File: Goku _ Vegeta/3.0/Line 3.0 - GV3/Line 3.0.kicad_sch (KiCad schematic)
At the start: 109 parts, among them J1 BATTERY POWER, J10 RIGHT HEADERS, J11 I2C, J3 Motor 1, J4 Motor 3, J5 Kicker Voltmeter, J6 Solenoid, J7 Motor 2, J8 Motor 4, J9 LEFT HEADERS, Q1 BSC040N10NS5, U1 TPS62132, U2 TPS62133, U4 TB67H420FTG Dual/Single Motor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, U5 TB67H420FTG Dual/Single Motor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, U6 LM2587S-ADJ, U7 TB67H420FTG Dual/Single Motor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, U8 TB67H420FTG Dual/Single Motor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, U9 DEV-16771

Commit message: Line 3.0 save
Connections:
- net SEN10 is gone; now on net 38: A10.2, R26.2
- net SEN11 is gone; now on net 39: A11.2, R27.2
- net SEN12 is gone; now on net 40: A12.2, R28.2
- net SEN13 is gone; now on net 41: A13.2, R29.2
- net SEN2 is gone; now on net 26: A2.2, R10.2
- net SEN3 is gone; now on net 24: A3.2, R11.2
- net SEN6 is gone; now on net 27: A6.2, R14.2
- net SEN7 is gone; now on net 25: A7.2, R15.2
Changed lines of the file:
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@@
     (effects (font (size 1.27 1.27)) (justify right bottom))
   )
-  (label "SEN11" (at 275.59 226.06 0) (fields_autoplaced)
-    (effects (font (size 1.27 1.27)) (justify left bottom))
+  (label "SEN11" (at 386.08 205.74 180) (fields_autoplaced)
+    (effects (font (size 1.27 1.27)) (justify right bottom))
   )
   (label "16" (at 327.66 200.66 0) (fields_autoplaced)
     (effects (font (size 1.27 1.27)) (justify left bottom))
   )
-  (label "SEN12" (at 275.59 228.6 0) (fields_autoplaced)
-    (effects (font (size 1.27 1.27)) (justify left bottom))
+  (label "SEN12" (at 386.08 203.2 180) (fields_autoplaced)
+    (effects (font (size 1.27 1.27)) (justify right bottom))
   )
   (label "30" (at 327.66 175.26 0) (fields_autoplaced)
@@
     (effects (font (size 1.27 1.27)) (justify left bottom))
   )
-  (label "SEN13" (at 275.59 231.14 0) (fields_autoplaced)
-    (effects (font (size 1.27 1.27)) (justify left bottom))
+  (label "SEN13" (at 386.08 200.66 180) (fields_autoplaced)
+    (effects (font (size 1.27 1.27)) (justify right bottom))
   )
   (label "41" (at 393.7 186.69 0) (fields_autoplaced)
@@
     (effects (font (size 1.27 1.27)) (justify left bottom))
   )
-  (label "SEN3" (at 275.59 205.74 0) (fields_autoplaced)
-    (effects (font (size 1.27 1.27)) (justify left bottom))
+  (label "SEN3" (at 386.08 218.44 180) (fields_autoplaced)
+    (effects (font (size 1.27 1.27)) (justify right bottom))
   )
   (label "12" (at 309.88 180.34 180) (fields_autoplaced)
@@
     (effects (font (size 1.27 1.27)) (justify left bottom))
   )
-  (label "SEN10" (at 275.59 223.52 0) (fields_autoplaced)
-    (effects (font (size 1.27 1.27)) (justify left bottom))
+  (label "SEN10" (at 386.08 208.28 180) (fields_autoplaced)
+    (effects (font (size 1.27 1.27)) (justify right bottom))
   )
   (label "M1ENCA" (at 275.59 180.34 0) (fields_autoplaced)
@@
     (effects (font (size 1.27 1.27)) (justify right bottom))
   )
-  (label "SEN7" (at 275.59 215.9 0) (fields_autoplaced)
-    (effects (font (size 1.27 1.27)) (justify left bottom))
+  (label "SEN7" (at 386.08 215.9 180) (fields_autoplaced)
+    (effects (font (size 1.27 1.27)) (justify right bottom))
   )
   (label "M3IN1" (at 275.59 254 0) (fields_autoplaced)
@@
     (effects (font (size 1.27 1.27)) (justify right bottom))
   )
-  (label "SEN2" (at 275.59 203.2 0) (fields_autoplaced)
-    (effects (font (size 1.27 1.27)) (justify left bottom))
+  (label "SEN2" (at 386.08 213.36 180) (fields_autoplaced)
+    (effects (font (size 1.27 1.27)) (justify right bottom))
   )
   (label "15" (at 393.7 176.53 0) (fields_autoplaced)
@@
     (effects (font (size 1.27 1.27)) (justify right bottom))
   )
-  (label "SEN6" (at 275.59 213.36 0) (fields_autoplaced)
-    (effects (font (size 1.27 1.27)) (justify left bottom))
+  (label "SEN6" (at 386.08 210.82 180) (fields_autoplaced)
+    (effects (font (size 1.27 1.27)) (justify right bottom))
   )
   (label "10" (at 309.88 175.26 180) (fields_autoplaced)

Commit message: CLEAN UP 3.0 LINE SCH
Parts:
- added J2: BACKUP 5V, Connector_AMASS:AMASS_XT30U-F_1x02_P5.0mm_Vertical, symbol Connector:Conn_01x02_Male
- added J3: BACKUP 3V3, Connector_AMASS:AMASS_XT30U-F_1x02_P5.0mm_Vertical, symbol Connector:Conn_01x02_Male
- renumbered C11 to C10, C12 to C11, C13 to C12, C14 to C13, C6 to C5, C7 to C6, C8 to C7, C9 to C8, C10 to C9, J8 to J10, J9 to J11, J10 to J12, J11 to J4, J3 to J7, J7 to J8, J4 to J9, R34 to R33, R35 to R34, R36 to R35, R37 to R36, R38 to R37, R39 to R38, U6 to U3, U7 to U5, U5 to U6, U8 to U7, U9 to U8
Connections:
- net KICKERTRIG is gone; now on net 13: Q1.4 (G)
- net M1ENCA is gone; now on net 7: J7.5 (Pin_5)
- net M1ENCB is gone; now on net 8: J7.6 (Pin_6)
- net M1IN1 is gone; now on net 2: U4.4 (INA1)
- net M1IN2 is gone; now on net 6: U4.5 (INA2)
- net M1PWM is gone; now on net 28: U4.6 (PWMA)
- net M2ENCA is gone; now on net 34: J8.5 (Pin_5)
- net M2ENCB is gone; now on net 35: J8.6 (Pin_6)
- net M2IN1 is gone; now on net 9: U5.4 (INA1)
- net M2IN2 is gone; now on net 32: U5.5 (INA2)
- net M2PWM is gone; now on net 29: U5.6 (PWMA)
- net M3ENCA is gone; now on net 30: J9.5 (Pin_5)
- net M3ENCB is gone; now on net 31: J9.6 (Pin_6)
- net M3IN1 is gone; now on net 10: U6.4 (INA1)
- net M3IN2 is gone; now on net 12: U6.5 (INA2)
- net M3PWM is gone; now on net 37: U6.6 (PWMA)
- net M4ENCA is gone; now on net 3: J10.5 (Pin_5)
- net M4ENCB is gone; now on net 4: J10.6 (Pin_6)
- net M4IN1 is gone; now on net 11: U7.4 (INA1)
- net M4IN2 is gone; now on net 33: U7.5 (INA2)
- net M4PWM is gone; now on net 36: U7.6 (PWMA)
- net SEN14 is gone; now on net 14: A14.2, R30.2
- net SEN15 is gone; now on net 15: A15.2, R31.2
- net +15V: now also J2.1 (Pin_1), J3.1 (Pin_1)
- net GND: now also C2.2, C4.2, C6.1, U2.6 (AGND), U2.7 (FSW), U2.8 (DEF), J2.2 (Pin_2), J3.2 (Pin_2)
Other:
- moved on the sheet: C1, C10, C11, C12, C13, C2, C3, C4, C5, C6, C7, C8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

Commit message: line 3.0 - good for the night
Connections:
- net +15V: now also J1.2 (Pin_2); no longer J1.1 (Pin_1), J2.1 (Pin_1), J3.1 (Pin_1)
- net +3V3: now also J3.2 (Pin_2)
- net +5V: now also J2.2 (Pin_2)
- net 18: now also J4.2 (Pin_2); no longer J4.1 (Pin_1)
- net 19: now also J4.1 (Pin_1); no longer J4.2 (Pin_2)
- net GND: now also J1.1 (Pin_1), J2.1 (Pin_1), J3.1 (Pin_1); no longer J1.2 (Pin_2), J2.2 (Pin_2), J3.2 (Pin_2)
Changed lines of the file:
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@@
     (fill (type none))
   )
-  (rectangle (start 107.95 19.05) (end 139.7 67.31)
+  (rectangle (start 107.95 19.05) (end 139.7 68.58)
     (stroke (width 0) (type dash))
     (fill (type none))
@@
     )
   )
-  (symbol (lib_id "power:+15V") (at 130.81 53.34 0) (unit 1)
-    (in_bom yes) (on_board yes) (dnp no)
-    (property "Reference" "#PWR053" (at 130.81 57.15 0)
-      (effects (font (size 1.27 1.27)) hide)
-    )
-    (property "Value" "+15V" (at 130.81 49.53 0)
-      (effects (font (size 1.27 1.27)))
-    )
-    (property "Footprint" "" (at 130.81 53.34 0)
-      (effects (font (size 1.27 1.27)) hide)
-    )
-    (property "Datasheet" "" (at 130.81 53.34 0)
-      (effects (font (size 1.27 1.27)) hide)
-    )
-    (pin "1")
-    (instances
-      (project "Line 3.0"
-        (path "/d5c7bd24-918a-4dd6-9ba7-d38579daba08"
-          (reference "#PWR053") (unit 1)
-        )
-      )
-    )
-  )
   (symbol (lib_id "JB2835AWT-W-U30GA0000-N0000001:JB2835AWT-W-U30GA0000-N0000001") (at 24.13 252.73 90) (mirror x) (unit 1)
     (in_bom yes) (on_board yes) (dnp no)
@@
     )
   )
-  (symbol (lib_id "Connector:Conn_01x02_Male") (at 118.11 40.64 0) (unit 1)
-    (in_bom yes) (on_board yes) (dnp no) (fields_autoplaced)
-    (property "Reference" "J2" (at 118.745 35.56 0)
+  (symbol (lib_id "Connector:Conn_01x02_Male") (at 118.11 43.18 0) (mirror x) (unit 1)
+    (in_bom yes) (on_board yes) (dnp no)
+    (property "Reference" "J2" (at 118.11 38.1 0)
       (effects (font (size 1.27 1.27)))
     )
-    (property "Value" "BACKUP 5V" (at 118.745 38.1 0)
+    (property "Value" "BACKUP 5V" (at 118.11 35.56 0)
       (effects (font (size 1.27 1.27)))
     )
-    (property "Footprint" "Connector_AMASS:AMASS_XT30U-F_1x02_P5.0mm_Vertical" (at 118.11 40.64 0)
+    (property "Footprint" "Connector_AMASS:AMASS_XT30U-F_1x02_P5.0mm_Vertical" (at 118.11 43.18 0)
       (effects (font (size 1.27 1.27)) hide)
     )
-    (property "Datasheet" "~" (at 118.11 40.64 0)
+    (property "Datasheet" "~" (at 118.11 43.18 0)
       (effects (font (size 1.27 1.27)) hide)
     )
@@
     )
   )
+  (symbol (lib_id "power:+3V3") (at 130.81 53.34 0) (unit 1)
+    (in_bom yes) (on_board yes) (dnp no)
+    (property "Reference" "#PWR051" (at 130.81 57.15 0)
+      (effects (font (size 1.27 1.27)) hide)
+    )
+    (property "Value" "+3V3" (at 130.81 49.53 0)
+      (effects (font (size 1.27 1.27)))
+    )
+    (property "Footprint" "" (at 130.81 53.34 0)
+      (effects (font (size 1.27 1.27)) hide)
+    )
+    (property "Datasheet" "" (at 130.81 53.34 0)
+      (effects (font (size 1.27 1.27)) hide)
+    )
+    (pin "1")
+    (instances
+      (project "Line 3.0"
+        (path "/d5c7bd24-918a-4dd6-9ba7-d38579daba08"
+          (reference "#PWR051") (unit 1)
+        )
+      )
+    )
+  )
   (symbol (lib_id "Device:R_Small_US") (at 24.13 91.44 0) (unit 1)
     (in_bom yes) (on_board yes) (dnp no)
@@
     )
   )
-  (symbol (lib_id "Connector:Conn_01x02_Male") (at 118.11 27.94 0) (unit 1)
-    (in_bom yes) (on_board yes) (dnp no) (fields_autoplaced)
-    (property "Reference" "J1" (at 118.745 22.86 0)
+  (symbol (lib_id "Connector:Conn_01x02_Male") (at 118.11 30.48 0) (mirror x) (unit 1)
+    (in_bom yes) (on_board yes) (dnp no)
+    (property "Reference" "J1" (at 117.475 25.4 0)
       (effects (font (size 1.27 1.27)))
     )
-    (property "Value" "BATTERY POWER" (at 118.745 25.4 0)
+    (property "Value" "BATTERY POWER" (at 118.11 21.59 0)
       (effects (font (size 1.27 1.27)))
     )
-    (property "Footprint" "Connector_AMASS:AMASS_XT60-F_1x02_P7.20mm_Vertical" (at 118.11 27.94 0)
+    (property "Footprint" "Connector_AMASS:AMASS_XT60-F_1x02_P7.20mm_Vertical" (at 118.11 30.48 0)
       (effects (font (size 1.27 1.27)) hide)
     )
-    (property "Datasheet" "~" (at 118.11 27.94 0)
+    (property "Datasheet" "~" (at 118.11 30.48 0)
       (effects (font (size 1.27 1.27)) hide)
     )
@@
     )
   )
+  (symbol (lib_name "+5V_1") (lib_id "power:+5V") (at 130.81 40.64 0) (unit 1)
+    (in_bom yes) (on_board yes) (dnp no)
+    (property "Reference" "#PWR053" (at 130.81 44.45 0)
+      (effects (font (size 1.27 1.27)) hide)
+    )
+    (property "Value" "+5V" (at 130.81 36.83 0)
+      (effects (font (size 1.27 1.27)))
+    )
+    (property "Footprint" "" (at 130.81 40.64 0)
+      (effects (font (size 1.27 1.27)) hide)
+    )
+    (property "Datasheet" "" (at 130.81 40.64 0)
+      (effects (font (size 1.27 1.27)) hide)
+    )
+    (pin "1")
+    (instances
+      (project "Line 3.0"
+        (path "/d5c7bd24-918a-4dd6-9ba7-d38579daba08"
+          (reference "#PWR053") (unit 1)
+        )
+      )
+    )
+  )
   (symbol (lib_id "ALS-PT19-315C_L177_TR8:ALS-PT19-315C{slash}L177{slash}TR8") (at 34.29 121.92 0) (mirror y) (unit 1)
     (in_bom yes) (on_board yes) (dnp no)
@@
     )
   )
-  (symbol (lib_id "Connector:Conn_01x02_Male") (at 118.11 64.77 0) (unit 1)
-    (in_bom yes) (on_board yes) (dnp no) (fields_autoplaced)
-    (property "Reference" "J4" (at 118.745 59.69 0)
+  (symbol (lib_id "Connector:Conn_01x02_Male") (at 118.11 67.31 0) (mirror x) (unit 1)
+    (in_bom yes) (on_board yes) (dnp no)
+    (property "Reference" "J4" (at 118.11 62.23 0)
       (effects (font (size 1.27 1.27)))
     )
-    (property "Value" "I2C" (at 118.745 62.23 0)
+    (property "Value" "I2C" (at 118.11 59.69 0)
       (effects (font (size 1.27 1.27)))
     )
-    (property "Footprint" "Connector_AMASS:AMASS_XT30U-F_1x02_P5.0mm_Vertical" (at 118.11 64.77 0)
+    (property "Footprint" "Connector_AMASS:AMASS_XT30U-F_1x02_P5.0mm_Vertical" (at 118.11 67.31 0)
       (effects (font (size 1.27 1.27)) hide)
     )
-    (property "Datasheet" "~" (at 118.11 64.77 0)
+    (property "Datasheet" "~" (at 118.11 67.31 0)
       (effects (font (size 1.27 1.27)) hide)
     )
@@
     )
   )
-  (symbol (lib_id "power:+15V") (at 130.81 40.64 0) (unit 1)
-    (in_bom yes) (on_board yes) (dnp no)
-    (property "Reference" "#PWR051" (at 130.81 44.45 0)
-      (effects (font (size 1.27 1.27)) hide)
-    )
-    (property "Value" "+15V" (at 130.81 36.83 0)
-      (effects (font (size 1.27 1.27)))
-    )
-    (property "Footprint" "" (at 130.81 40.64 0)
-      (effects (font (size 1.27 1.27)) hide)
-    )
-    (property "Datasheet" "" (at 130.81 40.64 0)
-      (effects (font (size 1.27 1.27)) hide)
-    )
-    (pin "1")
-    (instances
-      (project "Line 3.0"
-        (path "/d5c7bd24-918a-4dd6-9ba7-d38579daba08"
-          (reference "#PWR051") (unit 1)
-        )
-      )
-    )
-  )
-  (symbol (lib_id "Connector:Conn_01x02_Male") (at 118.11 53.34 0) (unit 1)
+  (symbol (lib_id "Connector:Conn_01x02_Male") (at 118.11 55.88 0) (mirror x) (unit 1)
     (in_bom yes) (on_board yes) (dnp no)
-    (property "Reference" "J3" (at 118.11 48.26 0)
+    (property "Reference" "J3" (at 118.11 50.8 0)
       (effects (font (size 1.27 1.27)))
     )
-    (property "Value" "BACKUP 3V3" (at 118.745 50.8 0)
+    (property "Value" "BACKUP 3V3" (at 118.745 48.26 0)
       (effects (font (size 1.27 1.27)))
     )
-    (property "Footprint" "Connector_AMASS:AMASS_XT30U-F_1x02_P5.0mm_Vertical" (at 118.11 53.34 0)
+    (property "Footprint" "Connector_AMASS:AMASS_XT30U-F_1x02_P5.0mm_Vertical" (at 118.11 55.88 0)
       (effects (font (size 1.27 1.27)) hide)
     )
-    (property "Datasheet" "~" (at 118.11 53.34 0)
+    (property "Datasheet" "~" (at 118.11 55.88 0)
       (effects (font (size 1.27 1.27)) hide)
     )

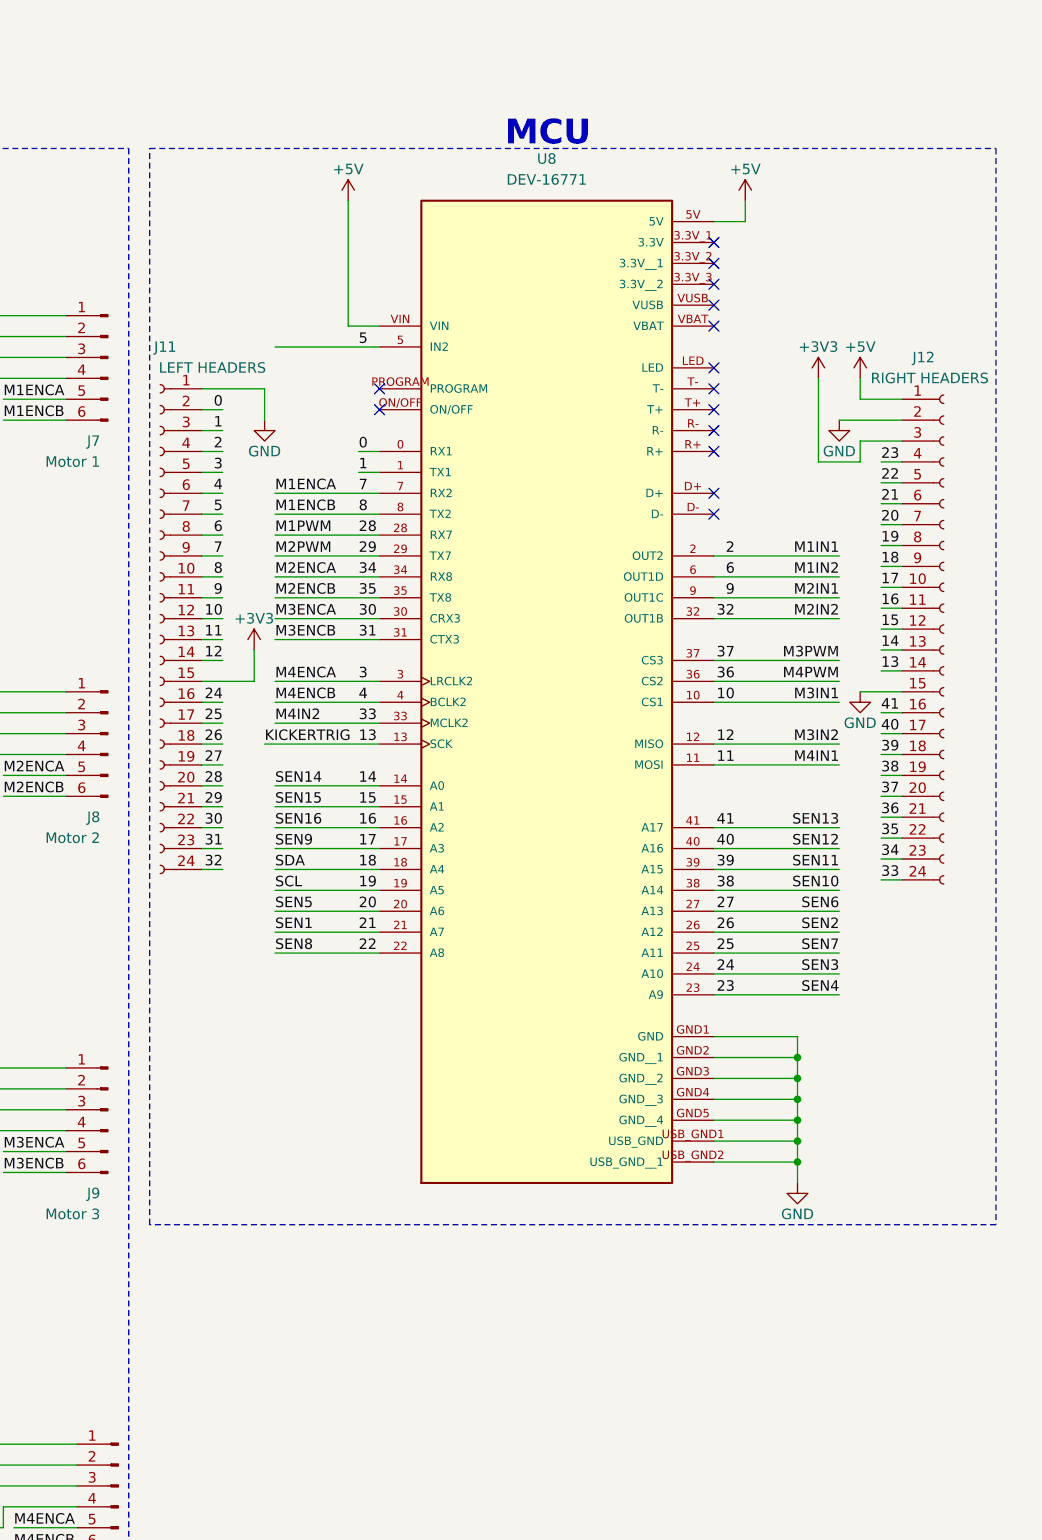
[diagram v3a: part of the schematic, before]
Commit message: LINE 3.0 - teensy - M driver routing +  added teensy programming. + on off switch breakout
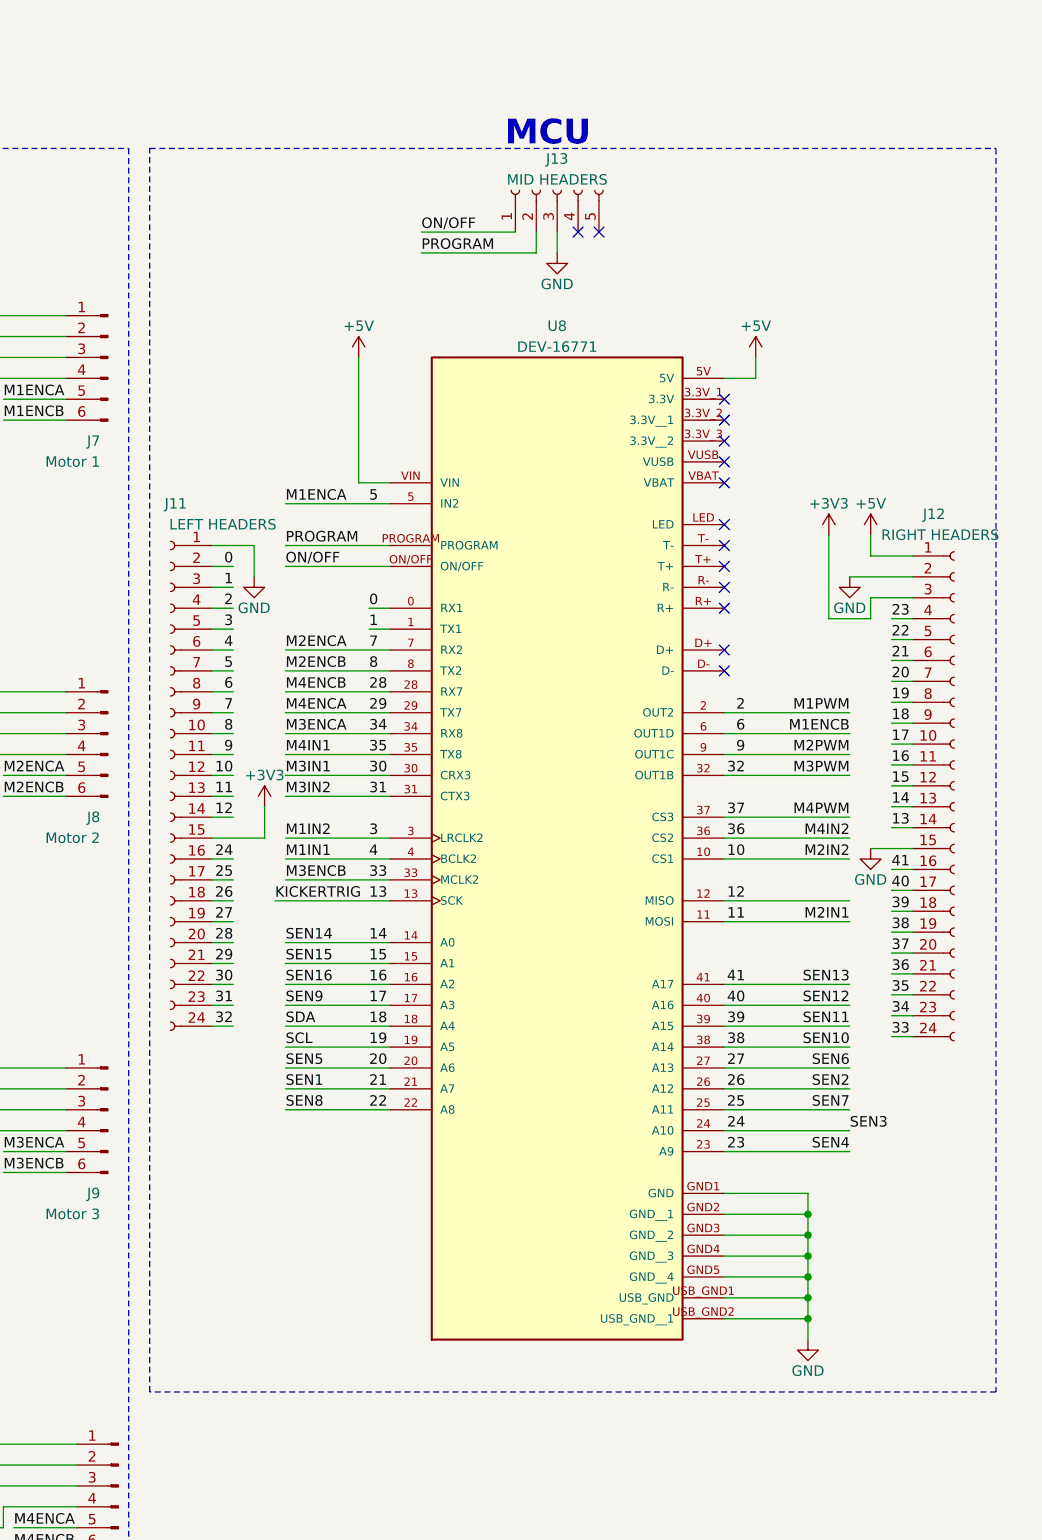
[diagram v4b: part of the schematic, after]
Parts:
- added J13: MID HEADERS, Connector_PinHeader_2.54mm:PinHeader_1x05_P2.54mm_Vertical, symbol Connector:Conn_01x05_Socket
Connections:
- net 10: now also U5.5 (INA2); no longer U6.4 (INA1)
- net 11: now also U5.4 (INA1); no longer U7.4 (INA1)
- net 12: no longer U6.5 (INA2)
- net 2: now also U4.6 (PWMA); no longer U4.4 (INA1)
- net 28: now also J10.6 (Pin_6); no longer U4.6 (PWMA)
- net 29: now also J10.5 (Pin_5); no longer U5.6 (PWMA)
- net 3: now also U4.5 (INA2); no longer J10.5 (Pin_5)
- net 30: now also U6.4 (INA1); no longer J9.5 (Pin_5)
- net 31: now also U6.5 (INA2); no longer J9.6 (Pin_6)
- net 32: now also U6.6 (PWMA); no longer U5.5 (INA2)
- net 33: now also J9.6 (Pin_6); no longer U7.5 (INA2)
- net 34: now also J9.5 (Pin_5); no longer J8.5 (Pin_5)
- net 35: now also U7.4 (INA1); no longer J8.6 (Pin_6)
- net 36: now also U7.5 (INA2); no longer U7.6 (PWMA)
- net 37: now also U7.6 (PWMA); no longer U6.6 (PWMA)
- net 4: now also U4.4 (INA1); no longer J10.6 (Pin_6)
- net 5: now also J7.5 (Pin_5)
- net 6: now also J7.6 (Pin_6); no longer U4.5 (INA2)
- net 7: now also J8.5 (Pin_5); no longer J7.5 (Pin_5)
- net 8: now also J8.6 (Pin_6); no longer J7.6 (Pin_6)
- net 9: now also U5.6 (PWMA); no longer U5.4 (INA1)
- net GND: now also J13.3 (Pin_3)
- net ON/OFF: now reaches U8.ON/OFF
- net ON/OFF: now also J13.1 (Pin_1)
- net PROGRAM: now reaches U8.PROGRAM
- net PROGRAM: now also J13.2 (Pin_2)
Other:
- moved on the sheet: J11, J12, U8

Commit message: LINE PCB 3.0 BASICALLY DONE!! NOW JUST GOTTA ADD SILKSCREEN!
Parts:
- removed C1, C2: 10uF, Capacitor_SMD:C_0805_2012Metric, symbol Device:C_Polarized_Small
- removed C3, C4: 0.1uF, Capacitor_SMD:C_0805_2012Metric, symbol Device:C_Polarized_Small
- removed C5, C6: 3.3nF, Capacitor_SMD:C_0805_2012Metric, symbol Device:C_Polarized_Small
- removed C7, C8: 22uF, Capacitor_SMD:C_0805_2012Metric, symbol Device:C_Polarized_Small
- removed D1, D2: STTH2002G-TR, Package_TO_SOT_SMD:TO-263-2, symbol Diode:STTH2002G
- removed J5: Kicker Voltmeter, TerminalBlock:TerminalBlock_bornier-2_P5.08mm, symbol Connector:Screw_Terminal_01x02
- removed L1, L2: 2.2uH, Inductor_SMD:L_Bourns_SRR1260, symbol Device:L
- removed R33, R34: 100K, Resistor_SMD:R_0805_2012Metric, symbol Device:R_Small
- removed U1: TPS62132, Package_DFN_QFN:VQFN-16-1EP_3x3mm_P0.5mm_EP1.68x1.68mm_ThermalVias, symbol Regulator_Switching:TPS62132
- removed U2: TPS62133, Package_DFN_QFN:VQFN-16-1EP_3x3mm_P0.5mm_EP1.68x1.68mm_ThermalVias, symbol Regulator_Switching:TPS62133
- added C14: 100uF, Capacitor_THT:CP_Radial_D10.0mm_P5.00mm, symbol Device:C_Polarized_Small
- added U1, U2: ~, Converter_DCDC:DC-DC Multi-output Buck Converter, symbol Converter_DCDC:DC-DC_Multi-output_Buck_Converter
- D3: footprint Diode_SMD:D_SOD-128 -> Diode_SMD:D_SMC
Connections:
- net +15V: now also U1.2 (IN+), U2.2 (IN+)
- net +3V3: now also U1.4 (OUT+)
- net +5V: now also U2.4 (OUT+)
- net 29: now also U6.6 (PWMA); no longer J10.5 (Pin_5)
- net 32: now also J10.5 (Pin_5); no longer U6.6 (PWMA)
- net GND: now also C14.2, U1.1 (IN-), U1.3 (OUT-), U2.1 (IN-), U2.3 (OUT-)
- net at C11.1, C12.1, C13.1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: now also C14.1
